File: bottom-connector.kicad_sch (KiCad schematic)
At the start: 6 parts, among them J4 Plug_Hirose_DF40_2x50_DF40C-1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, Q3 DZDH0401DW, Q9 AO3401A

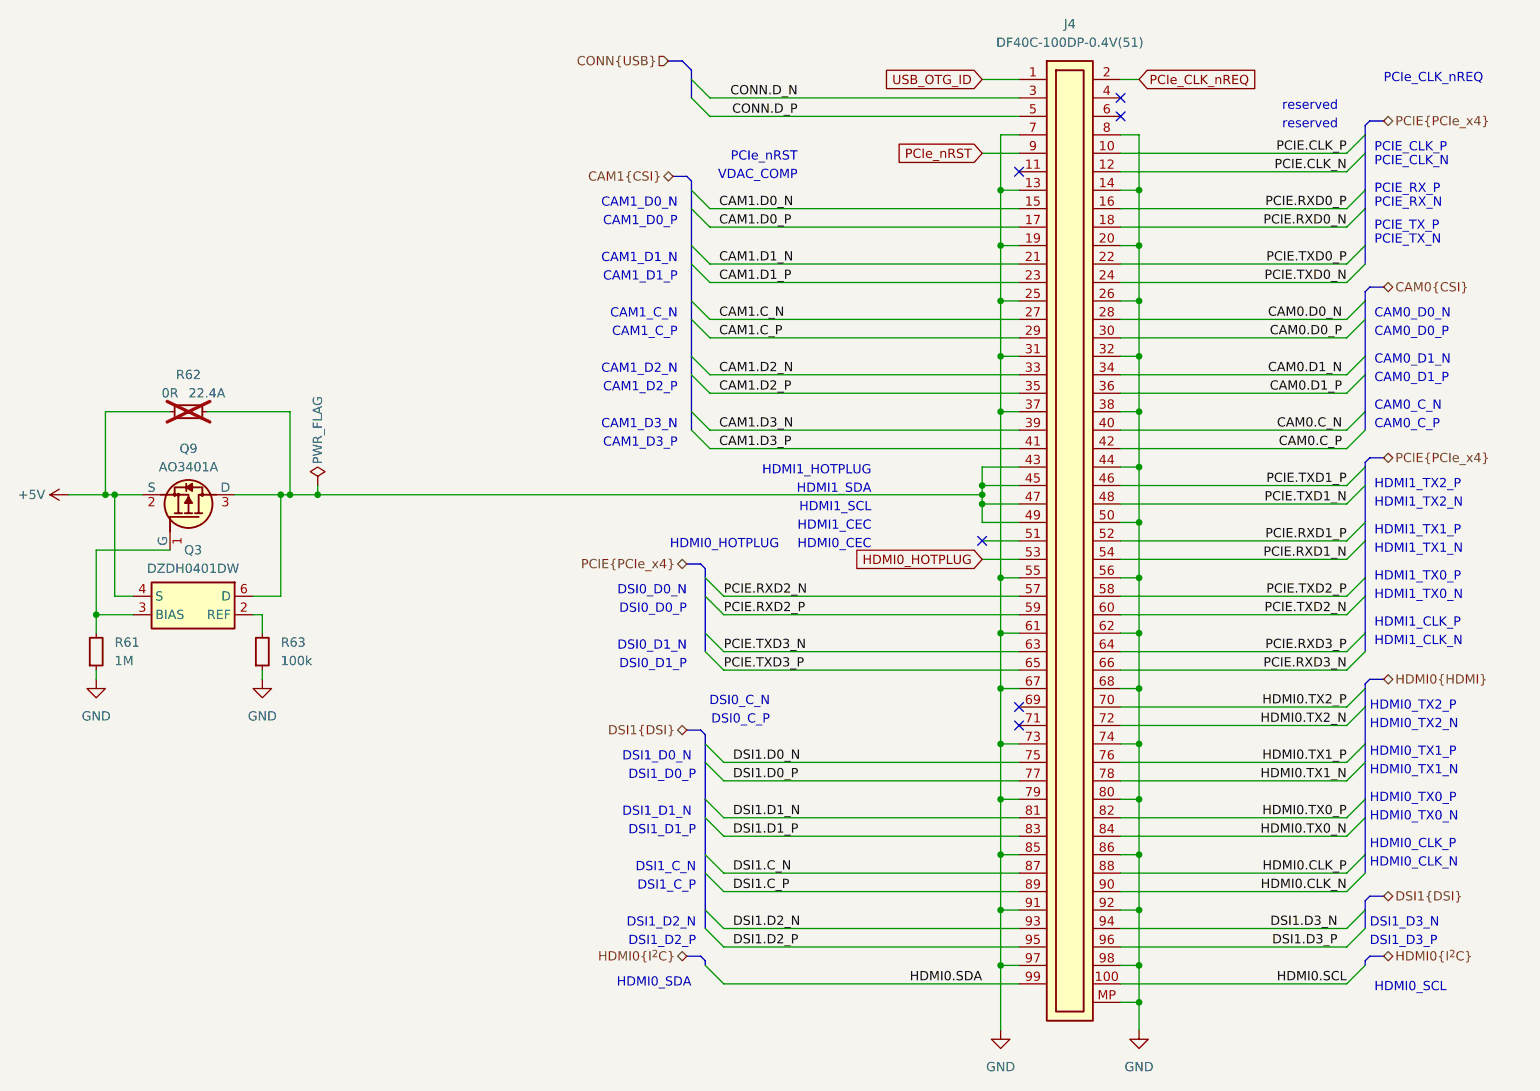
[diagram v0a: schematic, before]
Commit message: [#59910] Align buses, updated symbols and clean ERC
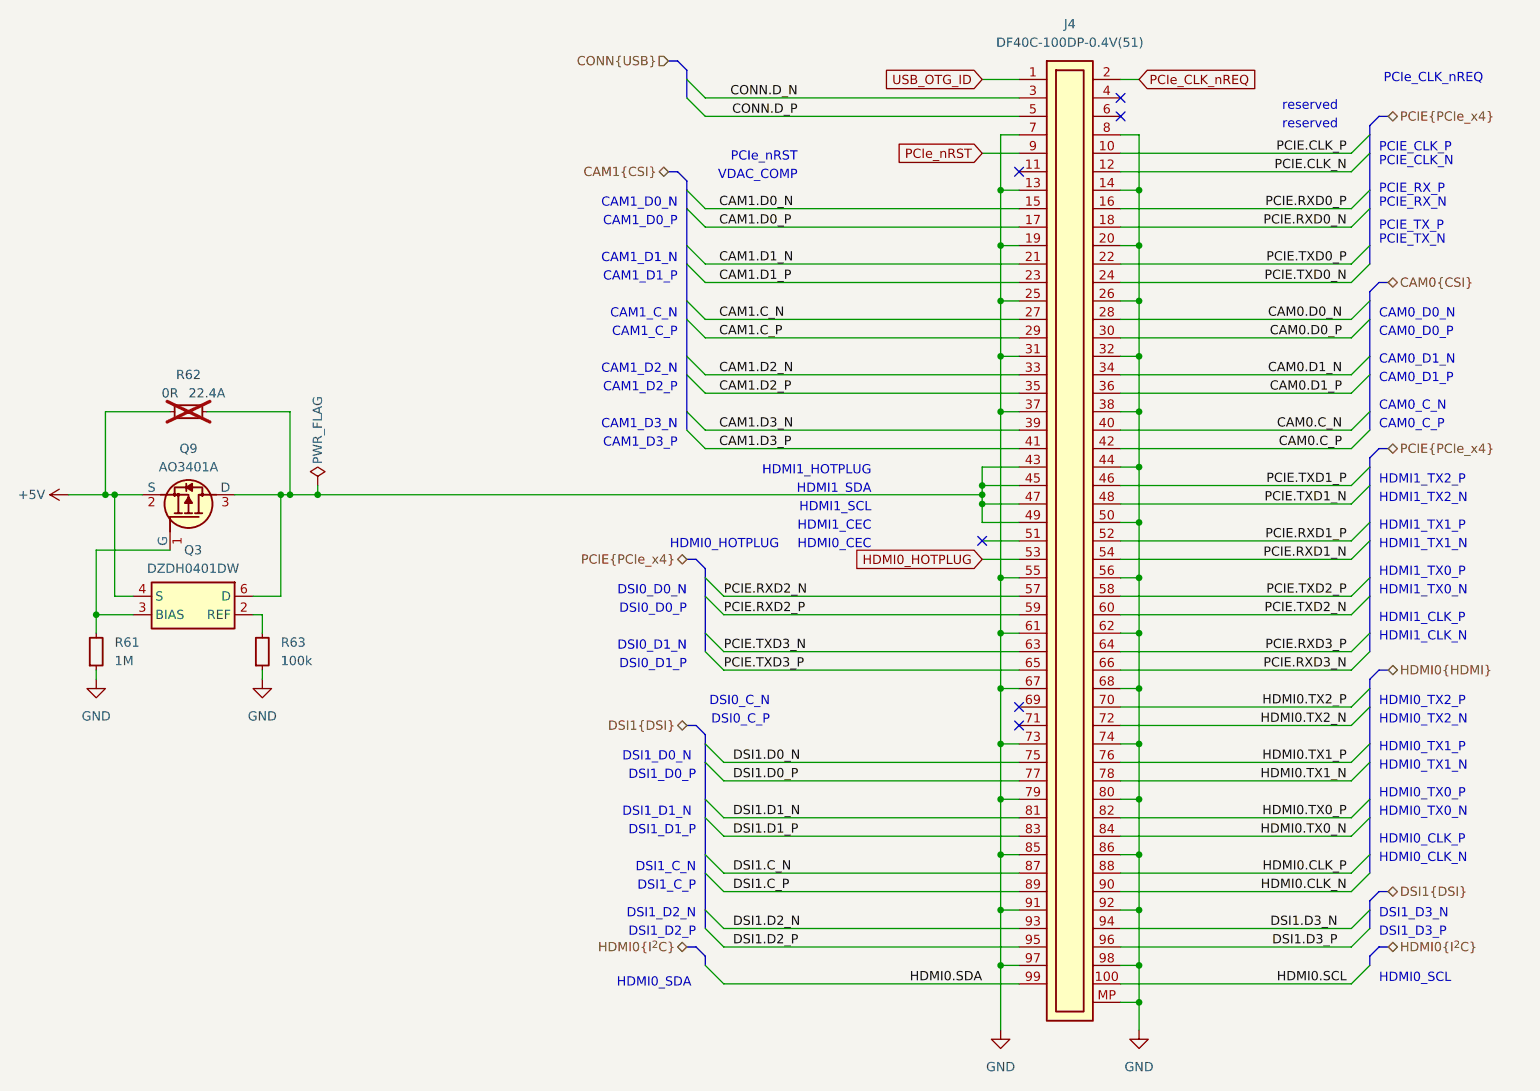
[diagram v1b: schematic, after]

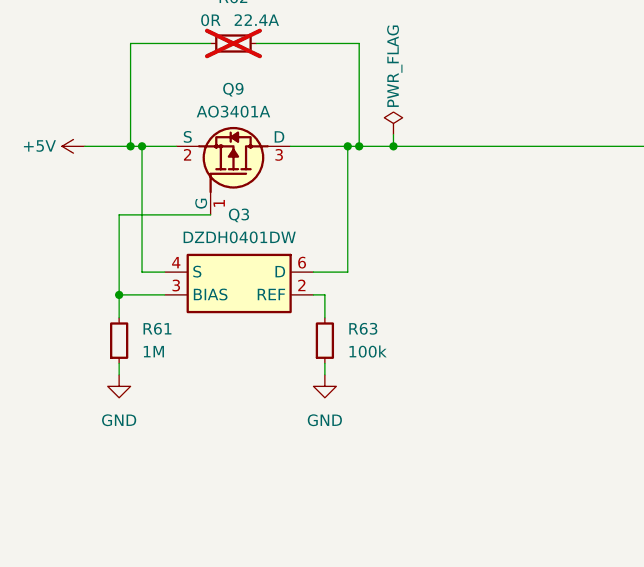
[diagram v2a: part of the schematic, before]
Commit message: [#73079] Update symbols, clean ERC
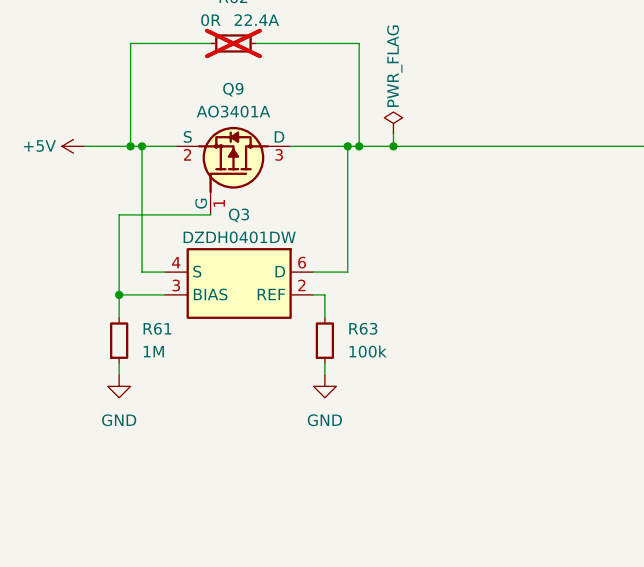
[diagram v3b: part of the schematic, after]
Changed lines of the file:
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@@
 	(label "CAM0.C_P"
 		(at 271.78 128.27 180)
+		(fields_autoplaced yes)
 		(effects
 			(font
@@
 	(label "CONN.D_P"
 		(at 196.85 82.55 180)
+		(fields_autoplaced yes)
 		(effects
 			(font
@@
 	(label "CAM1.D2_P"
 		(at 186.055 120.65 0)
+		(fields_autoplaced yes)
 		(effects
 			(font
@@
 	(label "HDMI0.SCL"
 		(at 272.415 201.93 180)
+		(fields_autoplaced yes)
 		(effects
 			(font
@@
 	(label "CAM1.C_N"
 		(at 186.055 110.49 0)
+		(fields_autoplaced yes)
 		(effects
 			(font
@@
 	(label "PCIE.RXD1_N"
 		(at 272.415 143.51 180)
+		(fields_autoplaced yes)
 		(effects
 			(font
@@
 	(label "PCIE.TXD3_N"
 		(at 186.69 156.21 0)
+		(fields_autoplaced yes)
 		(effects
 			(font
@@
 	(label "PCIE.TXD2_N"
 		(at 272.415 151.13 180)
+		(fields_autoplaced yes)
 		(effects
 			(font
@@
 	(label "CAM1.C_P"
 		(at 186.055 113.03 0)
+		(fields_autoplaced yes)
 		(effects
 			(font
@@
 	(label "CAM0.D0_N"
 		(at 271.78 110.49 180)
+		(fields_autoplaced yes)
 		(effects
 			(font
@@
 	(label "HDMI0.SDA"
 		(at 222.25 201.93 180)
+		(fields_autoplaced yes)
 		(effects
 			(font
@@
 	(label "DSI1.D0_P"
 		(at 187.96 173.99 0)
+		(fields_autoplaced yes)
 		(effects
 			(font
@@
 	(label "PCIE.TXD1_P"
 		(at 272.415 133.35 180)
+		(fields_autoplaced yes)
 		(effects
 			(font
@@
 	(label "CAM1.D0_N"
 		(at 186.055 95.25 0)
+		(fields_autoplaced yes)
 		(effects
 			(font
@@
 	(label "PCIE.TXD3_P"
 		(at 186.69 158.75 0)
+		(fields_autoplaced yes)
 		(effects
 			(font
@@
 	(label "HDMI0.CLK_N"
 		(at 272.415 189.23 180)
+		(fields_autoplaced yes)
 		(effects
 			(font
@@
 	(label "DSI1.C_N"
 		(at 187.96 186.69 0)
+		(fields_autoplaced yes)
 		(effects
 			(font
@@
 	(label "CAM1.D3_N"
 		(at 186.055 125.73 0)
+		(fields_autoplaced yes)
 		(effects
 			(font
@@
 	(label "DSI1.D2_P"
 		(at 187.96 196.85 0)
+		(fields_autoplaced yes)
 		(effects
 			(font
@@
 	(label "PCIE.RXD1_P"
 		(at 272.415 140.97 180)
+		(fields_autoplaced yes)
 		(effects
 			(font
@@
 	(label "HDMI0.TX2_N"
 		(at 272.415 166.37 180)
+		(fields_autoplaced yes)
 		(effects
 			(font
@@
 	(label "CAM1.D0_P"
 		(at 186.055 97.79 0)
+		(fields_autoplaced yes)
 		(effects
 			(font
@@
 	(label "DSI1.D1_N"
 		(at 187.96 179.07 0)
+		(fields_autoplaced yes)
 		(effects
 			(font
@@
 	(label "CAM0.D1_N"
 		(at 271.78 118.11 180)
+		(fields_autoplaced yes)
 		(effects
 			(font
@@
 	(label "DSI1.D2_N"
 		(at 187.96 194.31 0)
+		(fields_autoplaced yes)
 		(effects
 			(font
@@
 	(label "PCIE.RXD2_P"
 		(at 186.69 151.13 0)
+		(fields_autoplaced yes)
 		(effects
 			(font
@@
 	(label "PCIE.CLK_P"
 		(at 272.415 87.63 180)
+		(fields_autoplaced yes)
 		(effects
 			(font
@@
 	(label "HDMI0.CLK_P"
 		(at 272.415 186.69 180)
+		(fields_autoplaced yes)
 		(effects
 			(font
@@
 	(label "DSI1.C_P"
 		(at 187.96 189.23 0)
+		(fields_autoplaced yes)
 		(effects
 			(font
@@
 	(label "PCIE.TXD0_P"
 		(at 272.415 102.87 180)
+		(fields_autoplaced yes)
 		(effects
 			(font
@@
 	(label "DSI1.D3_P"
 		(at 271.145 196.85 180)
+		(fields_autoplaced yes)
 		(effects
 			(font
@@
 	(label "CAM1.D3_P"
 		(at 186.055 128.27 0)
+		(fields_autoplaced yes)
 		(effects
 			(font
@@
 	(label "HDMI0.TX0_N"
 		(at 272.415 181.61 180)
+		(fields_autoplaced yes)
 		(effects
 			(font
@@
 	(label "CAM0.D0_P"
 		(at 271.78 113.03 180)
+		(fields_autoplaced yes)
 		(effects
 			(font
@@
 	(label "HDMI0.TX0_P"
 		(at 272.415 179.07 180)
+		(fields_autoplaced yes)
 		(effects
 			(font
@@
 	(label "PCIE.RXD3_N"
 		(at 272.415 158.75 180)
+		(fields_autoplaced yes)
 		(effects
 			(font
@@
 	(label "PCIE.TXD0_N"
 		(at 272.415 105.41 180)
+		(fields_autoplaced yes)
 		(effects
 			(font
@@
 	(label "CAM1.D1_P"
 		(at 186.055 105.41 0)
+		(fields_autoplaced yes)
 		(effects
 			(font
@@
 	(label "CAM0.C_N"
 		(at 271.78 125.73 180)
+		(fields_autoplaced yes)
 		(effects
 			(font
@@
 	(label "HDMI0.TX2_P"
 		(at 272.415 163.83 180)
+		(fields_autoplaced yes)
 		(effects
 			(font
@@
 	(label "HDMI0.TX1_P"
 		(at 272.415 171.45 180)
+		(fields_autoplaced yes)
 		(effects
 			(font
@@
 	(label "PCIE.TXD1_N"
 		(at 272.415 135.89 180)
+		(fields_autoplaced yes)
 		(effects
 			(font
@@
 	(label "CONN.D_N"
 		(at 196.85 80.01 180)
+		(fields_autoplaced yes)
 		(effects
 			(font
@@
 	(label "PCIE.RXD2_N"
 		(at 186.69 148.59 0)
+		(fields_autoplaced yes)
 		(effects
 			(font
@@
 	(label "PCIE.TXD2_P"
 		(at 272.415 148.59 180)
+		(fields_autoplaced yes)
 		(effects
 			(font
@@
 	(label "PCIE.RXD0_N"
 		(at 272.415 97.79 180)
+		(fields_autoplaced yes)
 		(effects
 			(font
@@
 	(label "PCIE.CLK_N"
 		(at 272.415 90.17 180)
+		(fields_autoplaced yes)
 		(effects
 			(font
@@
 	(label "HDMI0.TX1_N"
 		(at 272.415 173.99 180)
+		(fields_autoplaced yes)
 		(effects
 			(font
@@
 	(label "PCIE.RXD0_P"
 		(at 272.415 95.25 180)
+		(fields_autoplaced yes)
 		(effects
 			(font
@@
 	(label "CAM1.D1_N"
 		(at 186.055 102.87 0)
+		(fields_autoplaced yes)
 		(effects
 			(font
@@
 	(label "DSI1.D0_N"
 		(at 187.96 171.45 0)
+		(fields_autoplaced yes)
 		(effects
 			(font
@@
 	(label "DSI1.D3_N"
 		(at 271.145 194.31 180)
+		(fields_autoplaced yes)
 		(effects
 			(font
@@
 	(label "CAM0.D1_P"
 		(at 271.78 120.65 180)
+		(fields_autoplaced yes)
 		(effects
 			(font
@@
 	(label "DSI1.D1_P"
 		(at 187.96 181.61 0)
+		(fields_autoplaced yes)
 		(effects
 			(font
@@
 	(label "PCIE.RXD3_P"
 		(at 272.415 156.21 180)
+		(fields_autoplaced yes)
 		(effects
 			(font
@@
 	(label "CAM1.D2_N"
 		(at 186.055 118.11 0)
+		(fields_autoplaced yes)
 		(effects
 			(font
@@
 		(shape bidirectional)
 		(at 278.13 189.23 0)
+		(fields_autoplaced yes)
 		(effects
 			(font
@@
 		(shape bidirectional)
 		(at 278.13 158.75 0)
+		(fields_autoplaced yes)
 		(effects
 			(font
@@
 		(shape bidirectional)
 		(at 278.13 128.27 0)
+		(fields_autoplaced yes)
 		(effects
 			(font
@@
 		(shape bidirectional)
 		(at 278.13 105.41 0)
+		(fields_autoplaced yes)
 		(effects
 			(font
@@
 		(shape input)
 		(at 179.07 74.93 180)
+		(fields_autoplaced yes)
 		(effects
 			(font
@@
 		(shape bidirectional)
 		(at 181.61 196.85 180)
+		(fields_autoplaced yes)
 		(effects
 			(font
@@
 		(shape bidirectional)
 		(at 181.61 166.37 180)
+		(fields_autoplaced yes)
 		(effects
 			(font
@@
 		(shape bidirectional)
 		(at 278.13 196.85 0)
+		(fields_autoplaced yes)
 		(effects
 			(font
@@
 		(shape bidirectional)
 		(at 181.61 143.51 180)
+		(fields_autoplaced yes)
 		(effects
 			(font
@@
 		(shape bidirectional)
 		(at 179.07 90.17 180)
+		(fields_autoplaced yes)
 		(effects
 			(font
@@
 		(shape bidirectional)
 		(at 278.13 82.55 0)
+		(fields_autoplaced yes)
 		(effects
 			(font
@@
 			)
 		)
-		(property "Description" ""
+		(property "Description" "SMD Chip Resistor"
 			(at 110.49 123.19 0)
 			(effects
@@
 			)
 		)
-		(property "Description" ""
+		(property "Description" "Mezzanine Connector, Header, 0.4 mm, 2 Rows, 100 Contacts, Surface Mount, Phosphor Bronze"
 			(at 227.33 77.47 0)
 			(effects
@@
 			)
 		)
-		(property "Description" ""
+		(property "Description" "OR Controller N+1 ORing Controller P-Channel 1:1 SOT-363"
 			(at 121.92 148.59 0)
 			(effects
@@
 		)
 		(pin "2"
+		)
+		(pin "1"
+		)
+		(pin "5"
 		)
 		(instances
@@
 			)
 		)
-		(property "Description" ""
+		(property "Description" "SMD Chip Resistor, 100 kohm, ± 1%, 62.5 mW, 0402 [1005 Metric], Thick Film, General Purpose"
 			(at 123.19 158.75 0)
 			(effects
@@
 			)
 		)
-		(property "Description" ""
+		(property "Description" "SMD Chip Resistor, 1 Mohm, ± 1%, 62.5 mW, 0402 [1005 Metric], Thick Film, General Purpose"
 			(at 100.33 158.75 0)
 			(effects
@@
 			)
 		)
-		(property "Description" ""
+		(property "Description" "Power MOSFET, P Channel, 30 V, 4 A, 0.07 ohm, SOT-23, Surface Mount"
 			(at 110.49 142.24 0)
 			(effects
